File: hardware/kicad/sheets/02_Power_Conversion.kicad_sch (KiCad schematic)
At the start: 0 parts

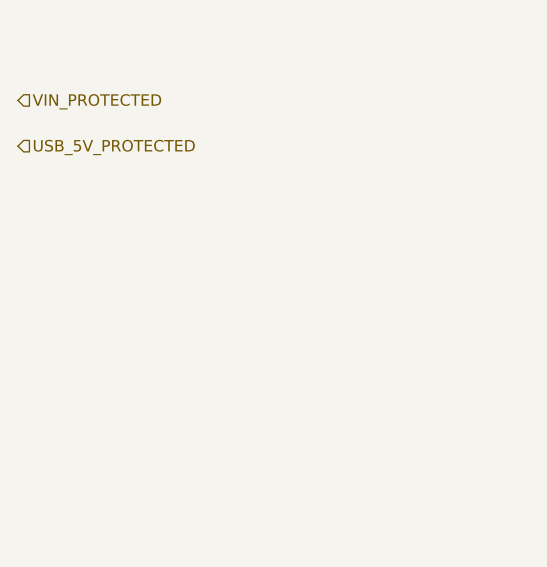
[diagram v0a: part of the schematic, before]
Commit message: Resolve Rev A power control interfaces
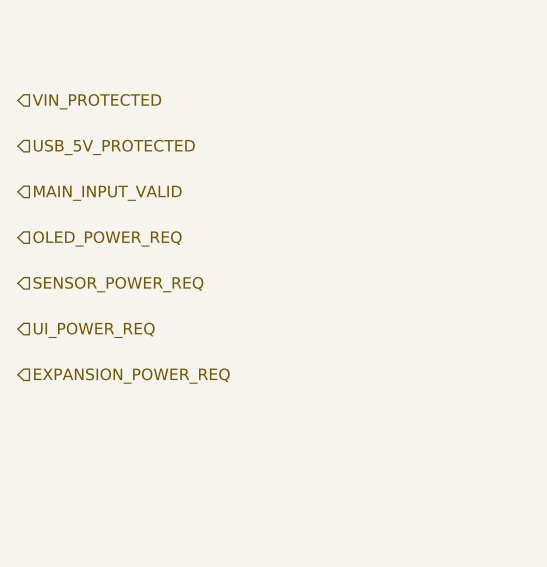
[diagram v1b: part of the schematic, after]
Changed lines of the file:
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@@
+    (effects (font (size 1.27 1.27)) (justify left))
+  )
+  (hierarchical_label "MAIN_INPUT_VALID" (shape input) (at 25.4 55.16 0)
+    (effects (font (size 1.27 1.27)) (justify left))
+  )
+  (hierarchical_label "OLED_POWER_REQ" (shape input) (at 25.4 60.24 0)
+    (effects (font (size 1.27 1.27)) (justify left))
+  )
+  (hierarchical_label "SENSOR_POWER_REQ" (shape input) (at 25.4 65.32 0)
+    (effects (font (size 1.27 1.27)) (justify left))
+  )
+  (hierarchical_label "UI_POWER_REQ" (shape input) (at 25.4 70.40 0)
+    (effects (font (size 1.27 1.27)) (justify left))
+  )
+  (hierarchical_label "EXPANSION_POWER_REQ" (shape input) (at 25.4 75.48 0)
     (effects (font (size 1.27 1.27)) (justify left))
   )

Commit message: Implement Rev A power conversion controls
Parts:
- added C1: 2.2 µF 100 V, symbol IPC100:C
- added C10: 10 nF soft start, symbol IPC100:C
- added C11, C13, C15, C18, C20: 1 nF slew control, symbol IPC100:C
- added C12, C14, C16, C17, C19, C21: 4.7 µF branch local, symbol IPC100:C
- added C2: 100 nF bootstrap, symbol IPC100:C
- added C3, C4, C8, C9: 22 µF 10 V, symbol IPC100:C
- added C5: 100 nF soft start, symbol IPC100:C
- added C6: 47 µF 10 V mux hold-up, symbol IPC100:C
- added C7: 10 µF 10 V, symbol IPC100:C
- added D1: 4.7 V EN clamp, symbol IPC100:D
- added D10, D3, D4, D5, D6, D7, D8, D9: Schottky reverse-injection block (TBD exact), symbol IPC100:D
- added D2: 3.3 V bias clamp, symbol IPC100:D
- added L1: 15 µH, ≥3.2 A Isat, ≤100 mΩ (TBD exact), symbol IPC100:L
- added L2: 2.2 µH, ≥4.0 A Isat, ≤60 mΩ (TBD exact), symbol IPC100:L
- added R1: 40.2 kΩ 1% — 400 kHz, symbol IPC100:R
- added R10: 316 kΩ 0.1%, symbol IPC100:R
- added R11, R2: 100 kΩ 0.1%, symbol IPC100:R
- added R12: 100 kΩ enable, symbol IPC100:R
- added R13, R17: 10 kΩ PGOOD pull-up, symbol IPC100:R
- added R14, R18, R19, R20, R21: 100 kΩ fail-low, symbol IPC100:R
- added R15: 10 kΩ main-bias pull-up, symbol IPC100:R
- added R16: 100 kΩ bias feed, symbol IPC100:R
- added R22, R23, R24: 287 kΩ 1% — 100 mA target (verify), symbol IPC100:R
- added R25, R26, R27, R28, R29: 1 kΩ QOD limit, symbol IPC100:R
- added R3: 24.9 kΩ 0.1%, symbol IPC100:R
- added R30: 23.7 kΩ 1% — USB OV2, symbol IPC100:R
- added R31, R6, R8: 5.00 kΩ 1%, symbol IPC100:R
- added R4: 100 kΩ, symbol IPC100:R
- added R5: 10.2 kΩ 1%, symbol IPC100:R
- added R7: 23.7 kΩ 1%, symbol IPC100:R
- added R9: 60.4 kΩ 1% — ≈2 A limit (verify), symbol IPC100:R
- added U1: LMR38020S-Q1 — 400 kHz, spread-spectrum (provisio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, symbol IPC100:IC10
- added U10: TPS22918-Q1 RELAY logic branch, symbol IPC100:IC10
- added U11: TPS22918-Q1 FIELD-SENSE branch, symbol IPC100:IC10
- added U12, U13: TPS2553-Q1 100 mA motor-logic protected switch (p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, symbol IPC100:IC10
- added U2: TPS2121RUXR priority power mux, symbol IPC100:IC10
- added U3: TPS62130RGTR adjustable 3 A buck, symbol IPC100:IC10
- added U4: SN74LVC1G08-Q1 — MAIN_INPUT_VALID AND MAIN_5V_PGO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, symbol IPC100:IC10
- added U5: SN74LVC08A-Q1 quad AND — request × MAIN_POWER_GOOD, symbol IPC100:QUAL4
- added U6: TPS22918-Q1 OLED load switch, symbol IPC100:IC10
- added U7: TPS22918-Q1 SENSOR load switch, symbol IPC100:IC10
- added U8: TPS22918-Q1 UI load switch, symbol IPC100:IC10
- added U9: TPS2553-Q1 EXPANSION 100 mA protected switch — OP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, symbol IPC100:IC10
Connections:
- net +3V3_CORE: now also C8.2, C9.2, L2.2, R10.1, R13.2, R17.2, U3.7 (P7), U4.2 (P2), U5.6 (OLED_EN), U6.5 (P5), U7.5 (P5), U9.5 (P5)
- net +5V_MAIN: now also C3.2, C4.2, L1.2, R2.1, R5.1, R7.1, U10.5 (P5), U11.5 (P5), U12.5 (P5), U13.5 (P5), U2.5 (P5), U8.5 (P5)
- net CORE_SOURCE: now also C6.2, C7.2, R12.1, U2.10 (P10), U3.5 (P5)
- net EXPANSION_POWER_REQ: now also R21.2, U5.2 (SENSOR_REQ)
- net EXPANSION_VCC: now also C17.2, D6.2
- net FIELD_SENSE_VCC: now also C21.2, D8.2
- net MAIN_INPUT_VALID: now also R14.2, R15.2, U4.5 (P5)
- net MAIN_POWER_GOOD: now also U10.4 (P4), U11.4 (P4), U12.4 (P4), U13.4 (P4), U4.10 (P10), U5.1 (OLED_REQ)
- net MOTOR_LOGIC_5V_A: now also D9.2
- net MOTOR_LOGIC_5V_B: now also D10.2
- net OLED_POWER_REQ: now also R18.2, U5.5 (MAIN_GOOD)
- net OLED_VCC: now also C12.2, D3.2
- net RELAY_VCC: now also C19.2, D7.2
- net SENSOR_POWER_REQ: now also R19.2, U5.4 (EXP_REQ)
- net SENSOR_VCC: now also C14.2, D4.2
- net UI_POWER_REQ: now also R20.2, U5.3 (UI_REQ)
- net UI_VCC: now also C16.2, D5.2
- net USB_5V_PROTECTED: now also R30.1, U2.4 (P4)
- net VIN_PROTECTED: now also C1.2, R16.1, R4.1, U1.5 (P5)
- new net CORE_BUCK_EN: R12.2, U3.4 (P4)
- new net CORE_FB: R10.2, R11.2, U3.9 (P9)
- new net CORE_PGOOD_OD: R13.1, U3.8 (P8)
- new net CORE_SS: C10.2, U3.2 (P2)
- new net CORE_SW: L2.1, U3.10 (P10)
- new net EXP_BRANCH_EN: U5.7 (SENSOR_EN), U9.4 (P4)
- new net EXP_ILIM: R22.2, U9.3 (P3)
- new net EXP_SW_OUT: D6.1, U9.10 (P10)
- new net GND: C1.1, C10.1, C11.1, C12.1, C13.1, C14.1, C15.1, C16.1, C17.1, C18.1, C19.1, C20.1, C21.1, C3.1, C4.1, C5.1, C6.1, C7.1, C8.1, C9.1, D1.1, D2.1, R1.1, R11.1, R14.1, R18.1, R19.1, R20.1, R21.1, R22.1, R23.1, R24.1, R3.1, R31.1, R6.1, R8.1, R9.1, U1.2 (P2), U1.7 (P7), U10.2 (P2), U10.6 (P6), U11.2 (P2), U11.6 (P6), U12.2 (P2), U12.6 (P6), U13.2 (P2), U13.6 (P6), U2.2 (P2), U2.6 (P6), U3.1 (P1), U3.3 (P3), U3.6 (P6), U4.1 (P1), U4.3 (P3), U6.2 (P2), U6.6 (P6), U7.2 (P2), U7.6 (P6), U8.2 (P2), U8.6 (P6), U9.2 (P2), U9.6 (P6)
- new net MAIN_5V_PGOOD_OD: R17.1, U1.8 (P8), U4.4 (P4)
- new net MAIN_BOOT: C2.2, U1.1 (P1)
- new net MAIN_BUCK_EN: D1.2, R4.2, U1.4 (P4)
- new net MAIN_BUCK_RT: R1.2, U1.3 (P3)
- new net MAIN_FB: R2.2, R3.2, U1.9 (P9)
- new net MAIN_SW: C2.1, L1.1, U1.10 (P10)
- new net MAIN_VALID_BIAS: D2.2, R15.1, R16.2
- new net MUX_ILM: R9.2, U2.8 (P8)
- new net MUX_OV1: R7.2, R8.2, U2.1 (P1)
- new net MUX_OV2: R30.2, R31.2, U2.7 (P7)
- new net MUX_PR1: R5.2, R6.2, U2.3 (P3)
- new net MUX_SS: C5.2, U2.9 (P9)
- new net OLED_BRANCH_EN: U5.10 (VCC), U6.4 (P4)
- new net SENSOR_BRANCH_EN: U5.9 (EXP_EN), U7.4 (P4)
- new net U10_CT: C18.2, U10.3 (P3)
- new net U10_QOD: R28.2, U10.9 (P9)
- new net U10_SW_OUT: D7.1, R28.1, U10.10 (P10)
- new net U11_CT: C20.2, U11.3 (P3)
- new net U11_QOD: R29.2, U11.9 (P9)
- new net U11_SW_OUT: D8.1, R29.1, U11.10 (P10)
- new net U12_ILIM: R23.2, U12.3 (P3)
- new net U12_SW_OUT: D9.1, U12.10 (P10)
- new net U13_ILIM: R24.2, U13.3 (P3)
- new net U13_SW_OUT: D10.1, U13.10 (P10)
- new net U6_CT: C11.2, U6.3 (P3)
- new net U6_QOD: R25.2, U6.9 (P9)
- new net U6_SW_OUT: D3.1, R25.1, U6.10 (P10)
- new net U7_CT: C13.2, U7.3 (P3)
- new net U7_QOD: R26.2, U7.9 (P9)
- new net U7_SW_OUT: D4.1, R26.1, U7.10 (P10)
- new net U8_CT: C15.2, U8.3 (P3)
- new net U8_QOD: R27.2, U8.9 (P9)
- new net U8_SW_OUT: D5.1, R27.1, U8.10 (P10)
- new net UI_BRANCH_EN: U5.8 (UI_EN), U8.4 (P4)
- no-connect marks 0 -> 33
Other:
- note added: "1 — +5 V MAIN SYNCHRONOUS BUCK"
- note added: "2 — MAIN/USB CORE SOURCE MUX"
- note added: "3 — +3V3 CORE SYNCHRONOUS BUCK"
- note added: "3.3 V setpoint ≈3.33 V from 316 kΩ / 100 kΩ pending tolerance review. CORE_POWER_GOOD_LOCAL is regulator diagnostic only; Sheet 03 supervisor owns safety-qualified core-good/reset semantics."
- note added: "4 — MAIN POWER-GOOD QUALIFICATION"
- note added: "5 — REQUEST QUALIFICATION (ALL REQUESTS HAVE 100 kΩ HARDWARE PULL-DOWNS)"
- note added: "6 — REQUEST-CONTROLLED PERIPHERAL BRANCHES"
- note added: "7 — HARDWARE-ENABLED MAIN-ONLY BRANCHES"
- note added: "All external branch series blocking devices are provisional. Verify forward drop, reverse leakage, hot-plug, fault energy, and minimum load voltage before release."
- note added: "CAPACITORS: 100 V input, 10 V on 5 V/3.3 V; verify MLCC DC-bias effective capacitance. Inductor saturation and DCR values are release blockers."
- note added: "Hardware branch power never authorizes an actuator. Sheet 06 retains ACTUATOR_PERMIT and relay/motor command gating."
- note added: "IN1 = +5V_MAIN and PR1 divider gives main priority above ≈3.22 V; CP2 is low. IN2 = protected USB. TPS2121 internal FETs provide reverse-current blocking."
- note added: "MAIN_POWER_GOOD is active-high 3.3 V logic and cannot assert from USB alone. Loss of either eFuse PGOOD/PGTH validity or U1 PGOOD forces it low."
- note added: "THERMAL/LAYOUT: no footprints assigned. U1 PowerPAD, U2/U3 exposed pads, switching loops, copper spreading, and thermal vias require package-specific review."
- note added: "U1 is internally compensated with fixed soft start. Keep CIN, bootstrap capacitor, SW loop, L1, and COUT tight; thermal pad/vias required."
- note added: "U5 logic representation is functional; exact package pin mapping and unused-input treatment are Package 04/03R detailed-review items."
- note added: "U9, R22, D6, and C17 are DNP by default. TPS2553-Q1 is provisional pending exact current-limit, reverse-current, and connector-fault review."
- note removed: "Detailed implementation intentionally deferred to subsequent engineering package."
- note removed: "PACKAGE 01 PLACEHOLDER — NO CIRCUITRY OR FOOTPRINTS"
- title: IPC-100 Rev A — 02 Power Conversion -> IPC-100 Rev A — 02 Power Conversion & Rail Control

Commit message: Normalize Rev A reference designators
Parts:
- renumbered C1 to C201, C2 to C202, C3 to C203, C4 to C204, C5 to C205, C6 to C206, C7 to C207, C8 to C208, C9 to C209, C10 to C210, C11 to C211, C12 to C212, C13 to C213, C14 to C214, C15 to C215, C16 to C216, C17 to C217, C18 to C218, C19 to C219, C20 to C220, C21 to C221, D1 to D201, D2 to D202, D3 to D203, D4 to D204, D5 to D205, D6 to D206, D7 to D207, D8 to D208, D9 to D209, D10 to D210, L1 to L201, L2 to L202, R1 to R201, R2 to R202, R3 to R203, R4 to R204, R5 to R205, R6 to R206, R7 to R207, R8 to R208, R9 to R209, R10 to R210, R11 to R211, R12 to R212, R13 to R213, R14 to R214, R15 to R215, R16 to R216, R17 to R217, R18 to R218, R19 to R219, R20 to R220, R21 to R221, R22 to R222, R23 to R223, R24 to R224, R25 to R225, R26 to R226, R27 to R227, R28 to R228, R29 to R229, R30 to R230, R31 to R231, U1 to U201, U2 to U202, U3 to U203, U4 to U204, U5 to U205, U6 to U206, U7 to U207, U8 to U208, U9 to U209, U10 to U210, U11 to U211, U12 to U212, U13 to U213

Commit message: Complete ECO-006 power compatibility remediation
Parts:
- C201: value 2.2 µF 100 V -> 2.2 uF nominal; >=1.0 uF effective at 55 V; >=100 V X7R; ripple >=0.2 A
- C203, C204: value 22 µF 10 V -> 22 uF nominal; >=15 uF effective at 5.25 V; >=16 V X7R; regulator-stable ESR
- C206: value 47 µF 10 V mux hold-up -> 47 uF nominal mux transition reservoir; >=30 uF effective at 5.25 V; >=10 V; not system hold-up
- C208, C209: value 22 µF 10 V -> 22 uF nominal; >=15 uF effective at 3.4 V; >=10 V X7R; regulator-stable ESR
- L201: value 15 µH, ≥3.2 A Isat, ≤100 mΩ (TBD exact) -> 15 uH +/-20%; hot Isat >=3.2 A; Irms >=2.1 A; DCR <=100 mOhm; -40..125 C
- L202: value 2.2 µH, ≥4.0 A Isat, ≤60 mΩ (TBD exact) -> 2.2 uH +/-20%; hot Isat >=4.0 A; Irms >=1.6 A; DCR <=60 mOhm; -40..125 C
- U201: value LMR38020S-Q1 — 400 kHz, spread-spectrum (provisional suffix) -> 4.2..80 V synchronous buck class; 5.0 V/2 A; 400 kHz; spread-spectrum; PGOOD; Tj <=110 C (TBD exact)
- U203: value TPS62130RGTR adjustable 3 A buck -> 4.4..5.25 V synchronous buck class; 3.3 V/1.5 A continuous; >=2.5 A limit; ~2.5 MHz; Tj <=110 C
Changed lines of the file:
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@@
   (symbol (lib_id "IPC100:IC10") (at 80 50 0) (unit 1) (exclude_from_sim no) (in_bom yes) (on_board yes) (dnp no)
     (property "Reference" "U201" (at 80 34.76 0) (effects (font (size 1.27 1.27))))
-    (property "Value" "LMR38020S-Q1 — 400 kHz, spread-spectrum (provisional suffix)" (at 80 65.24 0) (effects (font (size 1.05 1.05))))
+    (property "Value" "4.2..80 V synchronous buck class; 5.0 V/2 A; 400 kHz; spread-spectrum; PGOOD; Tj <=110 C (TBD exact)" (at 80 65.24 0) (effects (font (size 0.78 0.78))))
     (property "Footprint" "" (at 80 50 0) (effects (font (size 1 1)) hide))
     (property "Datasheet" "https://www.ti.com/lit/ds/symlink/lmr38020-q1.pdf" (at 80 50 0) (effects (font (size 1 1)) hide))
@@
   (symbol (lib_id "IPC100:L") (at 120 39.84 0) (unit 1) (exclude_from_sim no) (in_bom yes) (on_board yes) (dnp no)
     (property "Reference" "L201" (at 120 36.34 0) (effects (font (size 1.1 1.1))))
-    (property "Value" "15 µH, ≥3.2 A Isat, ≤100 mΩ (TBD exact)" (at 120 43.34 0) (effects (font (size 0.95 0.95))))
+    (property "Value" "15 uH +/-20%; hot Isat >=3.2 A; Irms >=2.1 A; DCR <=100 mOhm; -40..125 C" (at 120 43.34 0) (effects (font (size 0.78 0.78))))
     (property "Footprint" "" (at 120 39.84 0) (effects (font (size 1 1)) hide))
     (property "Datasheet" "" (at 120 39.84 0) (effects (font (size 1 1)) hide))
@@
   (symbol (lib_id "IPC100:C") (at 45 55 90) (unit 1) (exclude_from_sim no) (in_bom yes) (on_board yes) (dnp no)
     (property "Reference" "C201" (at 45 51.5 90) (effects (font (size 1.1 1.1))))
-    (property "Value" "2.2 µF 100 V" (at 45 58.5 90) (effects (font (size 0.95 0.95))))
+    (property "Value" "2.2 uF nominal; >=1.0 uF effective at 55 V; >=100 V X7R; ripple >=0.2 A" (at 45 58.5 90) (effects (font (size 0.75 0.75))))
     (property "Footprint" "" (at 45 55 0) (effects (font (size 1 1)) hide))
     (property "Datasheet" "" (at 45 55 0) (effects (font (size 1 1)) hide))
@@
   (symbol (lib_id "IPC100:C") (at 135 58 90) (unit 1) (exclude_from_sim no) (in_bom yes) (on_board yes) (dnp no)
     (property "Reference" "C203" (at 135 54.5 90) (effects (font (size 1.1 1.1))))
-    (property "Value" "22 µF 10 V" (at 135 61.5 90) (effects (font (size 0.95 0.95))))
+    (property "Value" "22 uF nominal; >=15 uF effective at 5.25 V; >=16 V X7R; regulator-stable ESR" (at 135 61.5 90) (effects (font (size 0.75 0.75))))
     (property "Footprint" "" (at 135 58 0) (effects (font (size 1 1)) hide))
     (property "Datasheet" "" (at 135 58 0) (effects (font (size 1 1)) hide))
@@
   (symbol (lib_id "IPC100:C") (at 150 58 90) (unit 1) (exclude_from_sim no) (in_bom yes) (on_board yes) (dnp no)
     (property "Reference" "C204" (at 150 54.5 90) (effects (font (size 1.1 1.1))))
-    (property "Value" "22 µF 10 V" (at 150 61.5 90) (effects (font (size 0.95 0.95))))
+    (property "Value" "22 uF nominal; >=15 uF effective at 5.25 V; >=16 V X7R; regulator-stable ESR" (at 150 61.5 90) (effects (font (size 0.75 0.75))))
     (property "Footprint" "" (at 150 58 0) (effects (font (size 1 1)) hide))
     (property "Datasheet" "" (at 150 58 0) (effects (font (size 1 1)) hide))
@@
   (symbol (lib_id "IPC100:C") (at 285 58 90) (unit 1) (exclude_from_sim no) (in_bom yes) (on_board yes) (dnp no)
     (property "Reference" "C206" (at 285 54.5 90) (effects (font (size 1.1 1.1))))
-    (property "Value" "47 µF 10 V mux hold-up" (at 285 61.5 90) (effects (font (size 0.95 0.95))))
+    (property "Value" "47 uF nominal mux transition reservoir; >=30 uF effective at 5.25 V; >=10 V; not system hold-up" (at 285 61.5 90) (effects (font (size 0.72 0.72))))
     (property "Footprint" "" (at 285 58 0) (effects (font (size 1 1)) hide))
     (property "Datasheet" "" (at 285 58 0) (effects (font (size 1 1)) hide))
@@
   (symbol (lib_id "IPC100:IC10") (at 365 52 0) (unit 1) (exclude_from_sim no) (in_bom yes) (on_board yes) (dnp no)
     (property "Reference" "U203" (at 365 36.76 0) (effects (font (size 1.27 1.27))))
-    (property "Value" "TPS62130RGTR adjustable 3 A buck" (at 365 67.24 0) (effects (font (size 1.05 1.05))))
+    (property "Value" "4.4..5.25 V synchronous buck class; 3.3 V/1.5 A continuous; >=2.5 A limit; ~2.5 MHz; Tj <=110 C" (at 365 67.24 0) (effects (font (size 0.78 0.78))))
     (property "Footprint" "" (at 365 52 0) (effects (font (size 1 1)) hide))
     (property "Datasheet" "https://www.ti.com/lit/ds/symlink/tps62130.pdf" (at 365 52 0) (effects (font (size 1 1)) hide))
@@
   (symbol (lib_id "IPC100:L") (at 405 41.84 0) (unit 1) (exclude_from_sim no) (in_bom yes) (on_board yes) (dnp no)
     (property "Reference" "L202" (at 405 38.34 0) (effects (font (size 1.1 1.1))))
-    (property "Value" "2.2 µH, ≥4.0 A Isat, ≤60 mΩ (TBD exact)" (at 405 45.34 0) (effects (font (size 0.95 0.95))))
+    (property "Value" "2.2 uH +/-20%; hot Isat >=4.0 A; Irms >=1.6 A; DCR <=60 mOhm; -40..125 C" (at 405 45.34 0) (effects (font (size 0.78 0.78))))
     (property "Footprint" "" (at 405 41.84 0) (effects (font (size 1 1)) hide))
     (property "Datasheet" "" (at 405 41.84 0) (effects (font (size 1 1)) hide))
@@
   (symbol (lib_id "IPC100:C") (at 420 60 90) (unit 1) (exclude_from_sim no) (in_bom yes) (on_board yes) (dnp no)
     (property "Reference" "C208" (at 420 56.5 90) (effects (font (size 1.1 1.1))))
-    (property "Value" "22 µF 10 V" (at 420 63.5 90) (effects (font (size 0.95 0.95))))
+    (property "Value" "22 uF nominal; >=15 uF effective at 3.4 V; >=10 V X7R; regulator-stable ESR" (at 420 63.5 90) (effects (font (size 0.75 0.75))))
     (property "Footprint" "" (at 420 60 0) (effects (font (size 1 1)) hide))
     (property "Datasheet" "" (at 420 60 0) (effects (font (size 1 1)) hide))
@@
   (symbol (lib_id "IPC100:C") (at 435 60 90) (unit 1) (exclude_from_sim no) (in_bom yes) (on_board yes) (dnp no)
     (property "Reference" "C209" (at 435 56.5 90) (effects (font (size 1.1 1.1))))
-    (property "Value" "22 µF 10 V" (at 435 63.5 90) (effects (font (size 0.95 0.95))))
+    (property "Value" "22 uF nominal; >=15 uF effective at 3.4 V; >=10 V X7R; regulator-stable ESR" (at 435 63.5 90) (effects (font (size 0.75 0.75))))
     (property "Footprint" "" (at 435 60 0) (effects (font (size 1 1)) hide))
     (property "Datasheet" "" (at 435 60 0) (effects (font (size 1 1)) hide))

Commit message: Complete ECO-007 power programming corrections
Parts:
- R201: value 40.2 kΩ 1% — 400 kHz -> 64.9 kΩ ±1%, ≤100 ppm/°C — LMR38020F-Q1 RT/SYNC, 400 kHz
- R222, R223, R224: value 287 kΩ 1% — 100 mA target (verify) -> 150 kΩ ±1%, ≤100 ppm/°C — TPS2553-Q1 ILIM; 154..209 mA calculated
- U201: value 4.2..80 V synchronous buck class; 5.0 V/2 A; 400 kHz; spread-spectrum; PGOOD; Tj <=110 C (TBD exact) -> LMR38020F-Q1 adjustable-frequency family; 4.2..80 V; 5.0 V/2 A; RT/SYNC-programmed 400 kHz; PGOOD; spread spectrum
- U209: value TPS2553-Q1 EXPANSION 100 mA protected switch — OPTIONAL/DNP -> TPS2553-Q1 active-high EXPANSION switch; 150 kΩ RILIM; OPTIONAL/DNP
- U212, U213: value TPS2553-Q1 100 mA motor-logic protected switch (provisional) -> TPS2553-Q1 active-high motor-logic switch; 150 kΩ RILIM; 154..209 mA
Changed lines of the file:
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@@
   (symbol (lib_id "IPC100:IC10") (at 80 50 0) (unit 1) (exclude_from_sim no) (in_bom yes) (on_board yes) (dnp no)
     (property "Reference" "U201" (at 80 34.76 0) (effects (font (size 1.27 1.27))))
-    (property "Value" "4.2..80 V synchronous buck class; 5.0 V/2 A; 400 kHz; spread-spectrum; PGOOD; Tj <=110 C (TBD exact)" (at 80 65.24 0) (effects (font (size 0.78 0.78))))
+    (property "Value" "LMR38020F-Q1 adjustable-frequency family; 4.2..80 V; 5.0 V/2 A; RT/SYNC-programmed 400 kHz; PGOOD; spread spectrum" (at 80 65.24 0) (effects (font (size 0.78 0.78))))
     (property "Footprint" "" (at 80 50 0) (effects (font (size 1 1)) hide))
     (property "Datasheet" "https://www.ti.com/lit/ds/symlink/lmr38020-q1.pdf" (at 80 50 0) (effects (font (size 1 1)) hide))
@@
   (symbol (lib_id "IPC100:R") (at 50 78 90) (unit 1) (exclude_from_sim no) (in_bom yes) (on_board yes) (dnp no)
     (property "Reference" "R201" (at 50 74.5 90) (effects (font (size 1.1 1.1))))
-    (property "Value" "40.2 kΩ 1% — 400 kHz" (at 50 81.5 90) (effects (font (size 0.95 0.95))))
+    (property "Value" "64.9 kΩ ±1%, ≤100 ppm/°C — LMR38020F-Q1 RT/SYNC, 400 kHz" (at 50 81.5 90) (effects (font (size 0.95 0.95))))
     (property "Footprint" "" (at 50 78 0) (effects (font (size 1 1)) hide))
     (property "Datasheet" "" (at 50 78 0) (effects (font (size 1 1)) hide))
@@
   (symbol (lib_id "IPC100:IC10") (at 455 155 0) (unit 1) (exclude_from_sim no) (in_bom yes) (on_board yes) (dnp yes)
     (property "Reference" "U209" (at 455 139.76 0) (effects (font (size 1.27 1.27))))
-    (property "Value" "TPS2553-Q1 EXPANSION 100 mA protected switch — OPTIONAL/DNP" (at 455 170.24 0) (effects (font (size 1.05 1.05))))
+    (property "Value" "TPS2553-Q1 active-high EXPANSION switch; 150 kΩ RILIM; OPTIONAL/DNP" (at 455 170.24 0) (effects (font (size 1.05 1.05))))
     (property "Footprint" "" (at 455 155 0) (effects (font (size 1 1)) hide))
-    (property "Datasheet" "" (at 455 155 0) (effects (font (size 1 1)) hide))
+    (property "Datasheet" "https://www.ti.com/lit/ds/symlink/tps2553-q1.pdf" (at 455 155 0) (effects (font (size 1 1)) hide))
     (pin "1")
     (pin "2")
@@
   (symbol (lib_id "IPC100:R") (at 450 185 90) (unit 1) (exclude_from_sim no) (in_bom yes) (on_board yes) (dnp yes)
     (property "Reference" "R222" (at 450 181.5 90) (effects (font (size 1.1 1.1))))
-    (property "Value" "287 kΩ 1% — 100 mA target (verify)" (at 450 188.5 90) (effects (font (size 0.95 0.95))))
+    (property "Value" "150 kΩ ±1%, ≤100 ppm/°C — TPS2553-Q1 ILIM; 154..209 mA calculated" (at 450 188.5 90) (effects (font (size 0.95 0.95))))
     (property "Footprint" "" (at 450 185 0) (effects (font (size 1 1)) hide))
     (property "Datasheet" "" (at 450 185 0) (effects (font (size 1 1)) hide))
@@
   (symbol (lib_id "IPC100:IC10") (at 255 245 0) (unit 1) (exclude_from_sim no) (in_bom yes) (on_board yes) (dnp no)
     (property "Reference" "U212" (at 255 229.76 0) (effects (font (size 1.27 1.27))))
-    (property "Value" "TPS2553-Q1 100 mA motor-logic protected switch (provisional)" (at 255 260.24 0) (effects (font (size 1.05 1.05))))
+    (property "Value" "TPS2553-Q1 active-high motor-logic switch; 150 kΩ RILIM; 154..209 mA" (at 255 260.24 0) (effects (font (size 1.05 1.05))))
     (property "Footprint" "" (at 255 245 0) (effects (font (size 1 1)) hide))
-    (property "Datasheet" "" (at 255 245 0) (effects (font (size 1 1)) hide))
+    (property "Datasheet" "https://www.ti.com/lit/ds/symlink/tps2553-q1.pdf" (at 255 245 0) (effects (font (size 1 1)) hide))
     (pin "1")
     (pin "2")
@@
   (symbol (lib_id "IPC100:R") (at 255 275 90) (unit 1) (exclude_from_sim no) (in_bom yes) (on_board yes) (dnp no)
     (property "Reference" "R223" (at 255 271.5 90) (effects (font (size 1.1 1.1))))
-    (property "Value" "287 kΩ 1% — 100 mA target (verify)" (at 255 278.5 90) (effects (font (size 0.95 0.95))))
+    (property "Value" "150 kΩ ±1%, ≤100 ppm/°C — TPS2553-Q1 ILIM; 154..209 mA calculated" (at 255 278.5 90) (effects (font (size 0.95 0.95))))
     (property "Footprint" "" (at 255 275 0) (effects (font (size 1 1)) hide))
     (property "Datasheet" "" (at 255 275 0) (effects (font (size 1 1)) hide))
@@
   (symbol (lib_id "IPC100:IC10") (at 355 245 0) (unit 1) (exclude_from_sim no) (in_bom yes) (on_board yes) (dnp no)
     (property "Reference" "U213" (at 355 229.76 0) (effects (font (size 1.27 1.27))))
-    (property "Value" "TPS2553-Q1 100 mA motor-logic protected switch (provisional)" (at 355 260.24 0) (effects (font (size 1.05 1.05))))
+    (property "Value" "TPS2553-Q1 active-high motor-logic switch; 150 kΩ RILIM; 154..209 mA" (at 355 260.24 0) (effects (font (size 1.05 1.05))))
     (property "Footprint" "" (at 355 245 0) (effects (font (size 1 1)) hide))
-    (property "Datasheet" "" (at 355 245 0) (effects (font (size 1 1)) hide))
+    (property "Datasheet" "https://www.ti.com/lit/ds/symlink/tps2553-q1.pdf" (at 355 245 0) (effects (font (size 1 1)) hide))
     (pin "1")
     (pin "2")
@@
   (symbol (lib_id "IPC100:R") (at 355 275 90) (unit 1) (exclude_from_sim no) (in_bom yes) (on_board yes) (dnp no)
     (property "Reference" "R224" (at 355 271.5 90) (effects (font (size 1.1 1.1))))
-    (property "Value" "287 kΩ 1% — 100 mA target (verify)" (at 355 278.5 90) (effects (font (size 0.95 0.95))))
+    (property "Value" "150 kΩ ±1%, ≤100 ppm/°C — TPS2553-Q1 ILIM; 154..209 mA calculated" (at 355 278.5 90) (effects (font (size 0.95 0.95))))
     (property "Footprint" "" (at 355 275 0) (effects (font (size 1 1)) hide))
     (property "Datasheet" "" (at 355 275 0) (effects (font (size 1 1)) hide))
